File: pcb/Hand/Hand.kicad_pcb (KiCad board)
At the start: 4 copper layers, 76.2 x 50.8 mm, 43 parts, among them J0 Conn_01x12_Ribbon_Top, J1 Conn_01x12_Ribbon_Bottom, J2 Conn_01x02_Feedback_Power, U1 CD74HC4067M96, U2 4754, U3 TCA9548A

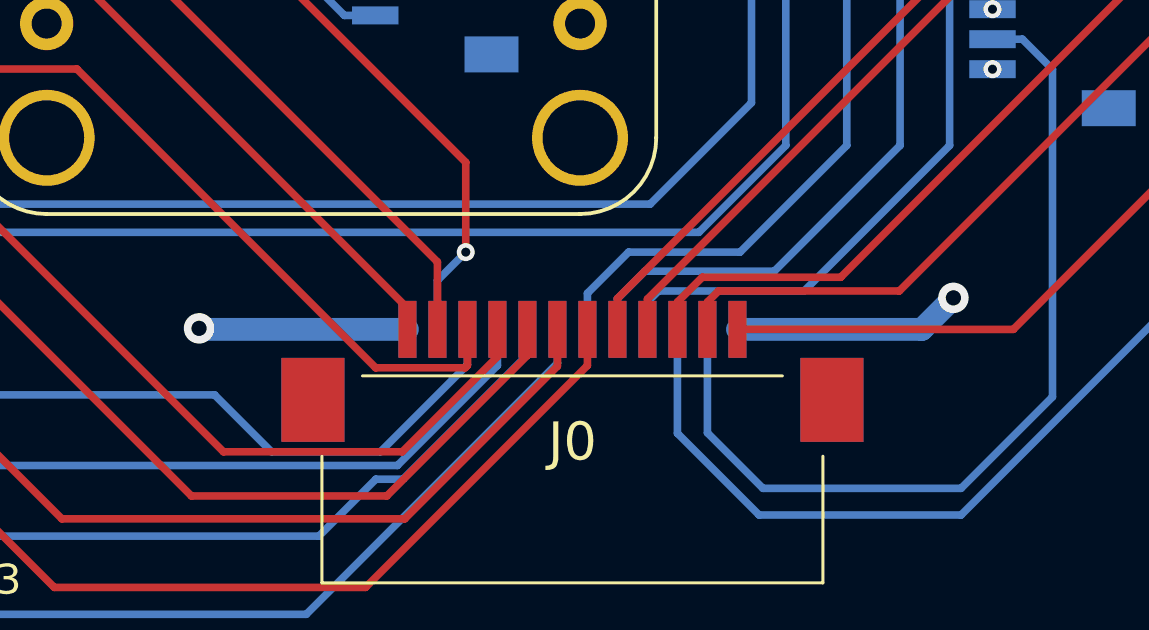
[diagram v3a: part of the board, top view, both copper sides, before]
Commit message: revised pcbs in preparation for pcb review; added pull-ups etc to forearm
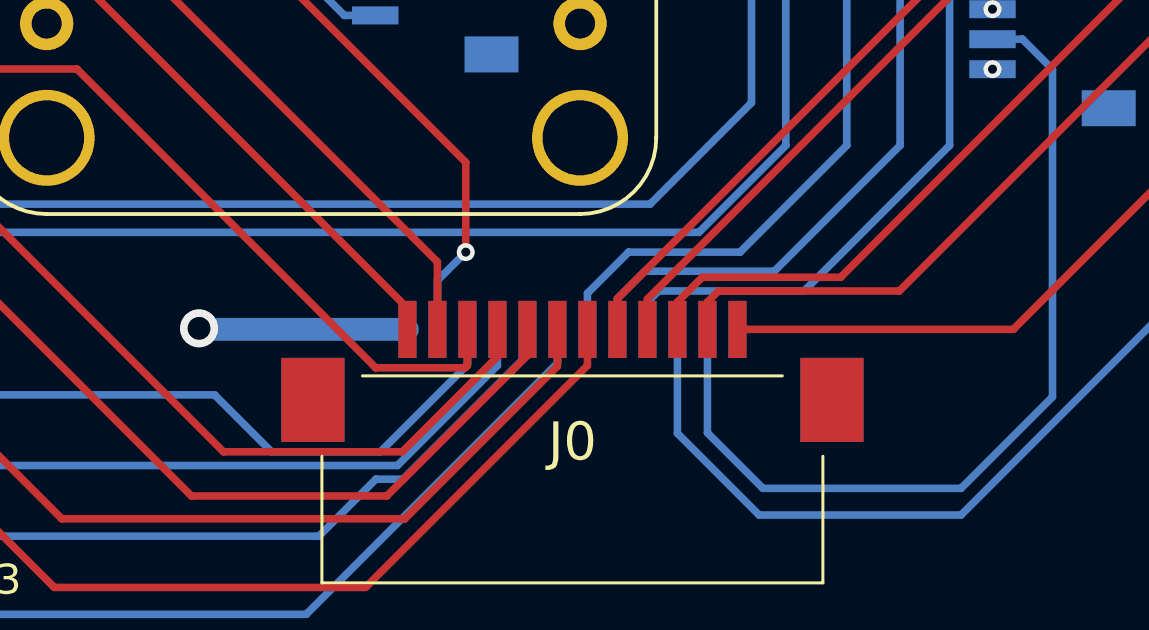
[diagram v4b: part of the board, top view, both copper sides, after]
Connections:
- FB0 pad 2: 6V0_GND -> GND
- FB1 pad 2: 6V0_GND -> GND
- FB2 pad 2: 6V0_GND -> GND
- FB3 pad 2: 6V0_GND -> GND
- FB4 pad 2: 6V0_GND -> GND
- J1 pad 1: GND -> FREE
- J2 pad 1: 6V0_GND -> GND
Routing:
- net GND: track 14.0 -> 6.37 mm, vias 29 -> 33
- net 6V0_GND: vias 5 -> 0
- removed copper zone on In2.Cu, net 6V0_GND
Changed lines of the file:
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@@
 	(net 50 "HALL_S1")
 	(net 51 "HALL_S3")
-	(net 52 "6V0_GND")
-	(net 53 "Net-(U1-~{E})")
-	(net 54 "unconnected-(U2-BT-PadJP2_1)")
-	(net 55 "unconnected-(U2-~{INT}-PadJP1_6)")
-	(net 56 "unconnected-(U2-~{RST}-PadJP2_4)")
-	(net 57 "unconnected-(U2-CS-PadJP2_6)")
-	(net 58 "unconnected-(U2-3VO-PadJP1_2)")
+	(net 52 "Net-(U1-~{E})")
+	(net 53 "unconnected-(U2-BT-PadJP2_1)")
+	(net 54 "unconnected-(U2-~{INT}-PadJP1_6)")
+	(net 55 "unconnected-(U2-~{RST}-PadJP2_4)")
+	(net 56 "unconnected-(U2-CS-PadJP2_6)")
+	(net 57 "unconnected-(U2-3VO-PadJP1_2)")
+	(net 58 "FREE")
 	(footprint "MountingHole:MountingHole_2.2mm_M2"
 		(layer "F.Cu")
@@
 			(size 0.6 1.55)
 			(layers "F.Cu" "F.Paste" "F.Mask")
-			(net 52 "6V0_GND")
+			(net 1 "GND")
 			(pinfunction "Pin_2")
 			(pintype "passive")
@@
 			(size 0.6 1.55)
 			(layers "F.Cu" "F.Paste" "F.Mask")
-			(net 52 "6V0_GND")
+			(net 1 "GND")
 			(pinfunction "Pin_2")
 			(pintype "passive")
@@
 			(layers "*.Cu" "*.Mask")
 			(remove_unused_layers no)
-			(net 52 "6V0_GND")
+			(net 1 "GND")
 			(pinfunction "Pin_1")
 			(pintype "passive")
@@
 			(size 0.6 1.55)
 			(layers "F.Cu" "F.Paste" "F.Mask")
-			(net 52 "6V0_GND")
+			(net 1 "GND")
 			(pinfunction "Pin_2")
 			(pintype "passive")
@@
 			(size 0.6 1.55)
 			(layers "F.Cu" "F.Paste" "F.Mask")
-			(net 52 "6V0_GND")
+			(net 1 "GND")
 			(pinfunction "Pin_2")
 			(pintype "passive")
@@
 			(size 0.6 1.55)
 			(layers "F.Cu" "F.Paste" "F.Mask")
-			(net 52 "6V0_GND")
+			(net 1 "GND")
 			(pinfunction "Pin_2")
 			(pintype "passive")
@@
 			(layers "*.Cu" "*.Mask")
 			(remove_unused_layers no)
-			(net 58 "unconnected-(U2-3VO-PadJP1_2)")
+			(net 57 "unconnected-(U2-3VO-PadJP1_2)")
 			(pinfunction "3VO")
 			(pintype "output")
@@
 			(layers "*.Cu" "*.Mask")
 			(remove_unused_layers no)
-			(net 55 "unconnected-(U2-~{INT}-PadJP1_6)")
+			(net 54 "unconnected-(U2-~{INT}-PadJP1_6)")
 			(pinfunction "~{INT}")
 			(pintype "output")
@@
 			(layers "*.Cu" "*.Mask")
 			(remove_unused_layers no)
-			(net 54 "unconnected-(U2-BT-PadJP2_1)")
+			(net 53 "unconnected-(U2-BT-PadJP2_1)")
 			(pinfunction "BT")
 			(pintype "input")
@@
 			(layers "*.Cu" "*.Mask")
 			(remove_unused_layers no)
-			(net 56 "unconnected-(U2-~{RST}-PadJP2_4)")
+			(net 55 "unconnected-(U2-~{RST}-PadJP2_4)")
 			(pinfunction "~{RST}")
 			(pintype "input")
@@
 			(layers "*.Cu" "*.Mask")
 			(remove_unused_layers no)
-			(net 57 "unconnected-(U2-CS-PadJP2_6)")
+			(net 56 "unconnected-(U2-CS-PadJP2_6)")
 			(pinfunction "CS")
 			(pintype "input")
@@
 			(layers "B.Cu" "B.Paste" "B.Mask")
 			(roundrect_rratio 0.125)
-			(net 53 "Net-(U1-~{E})")
+			(net 52 "Net-(U1-~{E})")
 			(pinfunction "~{E}")
 			(pintype "input")
@@
 			(size 0.6 1.9)
 			(layers "B.Cu" "B.Paste" "B.Mask")
-			(net 1 "GND")
+			(net 58 "FREE")
 			(pinfunction "Pin_1")
 			(pintype "passive")
@@
 			(layers "B.Cu" "B.Paste" "B.Mask")
 			(roundrect_rratio 0.25)
-			(net 53 "Net-(U1-~{E})")
+			(net 52 "Net-(U1-~{E})")
 			(pintype "passive")
 		)
@@
 	)
 	(via
+		(at 82.896 40.386)
+		(size 0.6)
+		(drill 0.3)
+		(layers "F.Cu" "B.Cu")
+		(net 1)
+	)
+	(via
 		(at 73.184 30.464)
 		(size 0.6)
@@
 	)
 	(via
+		(at 82.836 46.736)
+		(size 0.6)
+		(drill 0.3)
+		(layers "F.Cu" "B.Cu")
+		(net 1)
+	)
+	(via
 		(at 38.1508 28.702)
 		(size 0.6)
@@
 	)
 	(via
+		(at 82.896 34.036)
+		(size 0.6)
+		(drill 0.3)
+		(layers "F.Cu" "B.Cu")
+		(net 1)
+	)
+	(via
+		(at 82.836 21.336)
+		(size 0.6)
+		(drill 0.3)
+		(layers "F.Cu" "B.Cu")
+		(free yes)
+		(net 1)
+	)
+	(via
 		(at 45.75 17.591)
 		(size 0.6)
@@
 	)
 	(via
-		(at 71.882 51.816)
-		(size 1.016)
-		(drill 0.508)
+		(at 82.836 27.686)
+		(size 0.6)
+		(drill 0.3)
 		(layers "F.Cu" "B.Cu")
-		(free yes)
 		(net 1)
 	)
@@
 	)
 	(segment
-		(start 64.682 52.867)
-		(end 70.831 52.867)
-		(width 0.762)
-		(layer "B.Cu")
-		(net 1)
-	)
-	(segment
 		(start 18.163 26.289)
 		(end 17.1942 26.289)
@@
 	)
 	(segment
-		(start 70.831 52.867)
-		(end 71.882 51.816)
-		(width 0.762)
-		(layer "B.Cu")
-		(net 1)
-	)
-	(segment
 		(start 16.4208 28.6164)
 		(end 16.497 28.6926)
@@
 	(via
 		(at 46.736 52.832)
-		(size 1.016)
-		(drill 0.508)
+		(size 1.27)
+		(drill 0.762)
 		(layers "F.Cu" "B.Cu")
 		(free yes)
@@
 	)
 	(segment
-		(start 46.771 52.867)
-		(end 46.736 52.832)
-		(width 0.254)
+		(start 53.682 52.867)
+		(end 46.771 52.867)
+		(width 0.762)
 		(layer "B.Cu")
 		(net 2)
 	)
 	(segment
-		(start 53.682 52.867)
-		(end 46.771 52.867)
+		(start 46.771 52.867)
+		(end 46.736 52.832)
 		(width 0.762)
 		(layer "B.Cu")
@@
 		(net 51)
 	)
-	(via
-		(at 82.896 40.386)
-		(size 0.6)
-		(drill 0.3)
-		(layers "F.Cu" "B.Cu")
-		(net 52)
-	)
-	(via
-		(at 82.836 46.736)
-		(size 0.6)
-		(drill 0.3)
-		(layers "F.Cu" "B.Cu")
-		(net 52)
-	)
-	(via
-		(at 82.896 34.036)
-		(size 0.6)
-		(drill 0.3)
-		(layers "F.Cu" "B.Cu")
-		(net 52)
-	)
-	(via
-		(at 82.836 21.336)
-		(size 0.6)
-		(drill 0.3)
-		(layers "F.Cu" "B.Cu")
-		(net 52)
-	)
-	(via
-		(at 82.836 27.686)
-		(size 0.6)
-		(drill 0.3)
-		(layers "F.Cu" "B.Cu")
-		(net 52)
-	)
 	(segment
 		(start 24.3332 22.150699)
@@
 		(width 0.254)
 		(layer "B.Cu")
-		(net 53)
+		(net 52)
 	)
 	(segment
@@
 		(width 0.254)
 		(layer "B.Cu")
-		(net 53)
+		(net 52)
 	)
 	(segment
@@
 		(width 0.254)
 		(layer "B.Cu")
-		(net 53)
+		(net 52)
 	)
 	(zone
@@
 		(polygon
 			(pts
-				(xy 12.192 12.192) (xy 79.756 12.192) (xy 79.756 62.992) (xy 12.192 62.992)
-			)
-		)
-	)
-	(zone
-		(net 52)
-		(net_name "6V0_GND")
-		(layer "In2.Cu")
-		(hatch edge 0.5)
-		(priority 3)
-		(connect_pads
-			(clearance 0.5)
-		)
-		(min_thickness 0.25)
-		(filled_areas_thickness no)
-		(fill yes
-			(thermal_gap 0.5)
-			(thermal_bridge_width 0.5)
-		)
-		(polygon
-			(pts
-				(xy 80.264 12.192) (xy 80.264 62.992) (xy 88.392 62.992) (xy 88.392 12.192)
+				(xy 12.192 12.192) (xy 88.392 12.192) (xy 88.392 62.992) (xy 12.192 62.992)
 			)
 		)

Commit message: revised pcbs in prep for manufacture, rev2
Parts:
- removed J0: Conn_01x12_Ribbon_Top, 0522071233:0522071233
- removed J1: Conn_01x12_Ribbon_Bottom, 0522071233:0522071233
- added J3: Conn_01x16_Top, 522071633:CON_522071633_MOL, F.Cu at (61.2, 56.0)
- added J4: Conn_01x16_Bottom, 522071633:CON_522071633_MOL, B.Cu at (61.2, 56.0)
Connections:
- U2 pad JP1_6: unconnected-(U2-~{INT}-PadJP1_6) -> IMU_1_INT
- U2 pad JP2_4: unconnected-(U2-~{RST}-PadJP2_4) -> IMU_1_RST
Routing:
- net IMU_1_INT: track 0.00 -> 19.0 mm
- net IMU_1_RST: track 0.00 -> 16.4 mm
- net IMU_SCL: track 20.7 -> 35.1 mm
- net HAPTIC_S2: track 24.8 -> 35.2 mm
- net IMU_SDA: track 17.7 -> 27.9 mm
- net HAPTIC_S1: track 26.9 -> 34.6 mm
- net HAPTIC_S0: track 28.0 -> 34.7 mm
- net FEEDBACK_D4: track 21.1 -> 17.0 mm
- net HAPTIC_SDA: track 29.6 -> 33.5 mm, vias 0 -> 2
- net FEEDBACK_D3: track 25.3 -> 21.4 mm
- net FEEDBACK_D2: track 31.3 -> 27.4 mm
- net HAPTIC_SCL: track 27.8 -> 30.8 mm, vias 0 -> 2
- net FEEDBACK_D1: track 36.1 -> 34.4 mm
- net FEEDBACK_D0: track 42.2 -> 40.5 mm
- net unconnected-(J3-Pin_1-Pad1): track 0.00 -> 0.71 mm

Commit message: hand boatd final?
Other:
- board text added: "Dexterity Hand JLL"

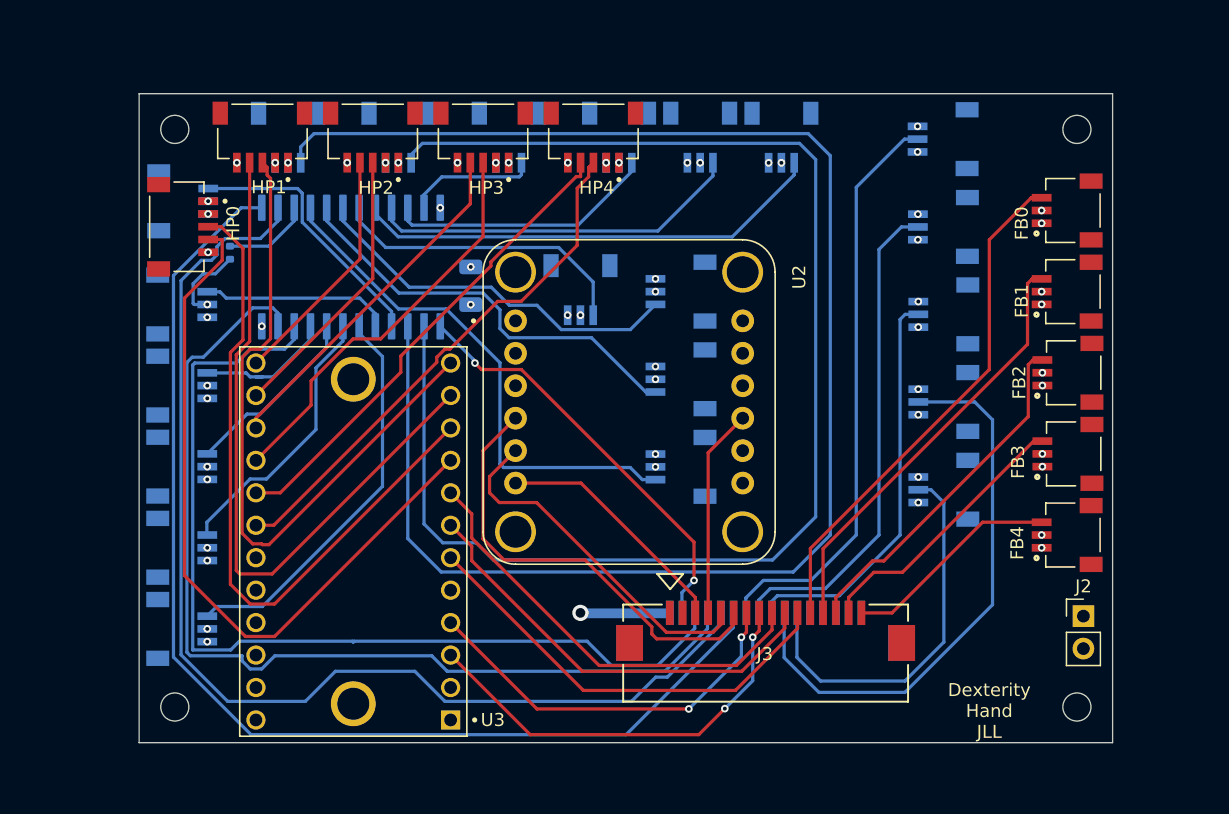
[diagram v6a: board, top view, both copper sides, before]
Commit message: added ground pours and generated gerbers for pcbs
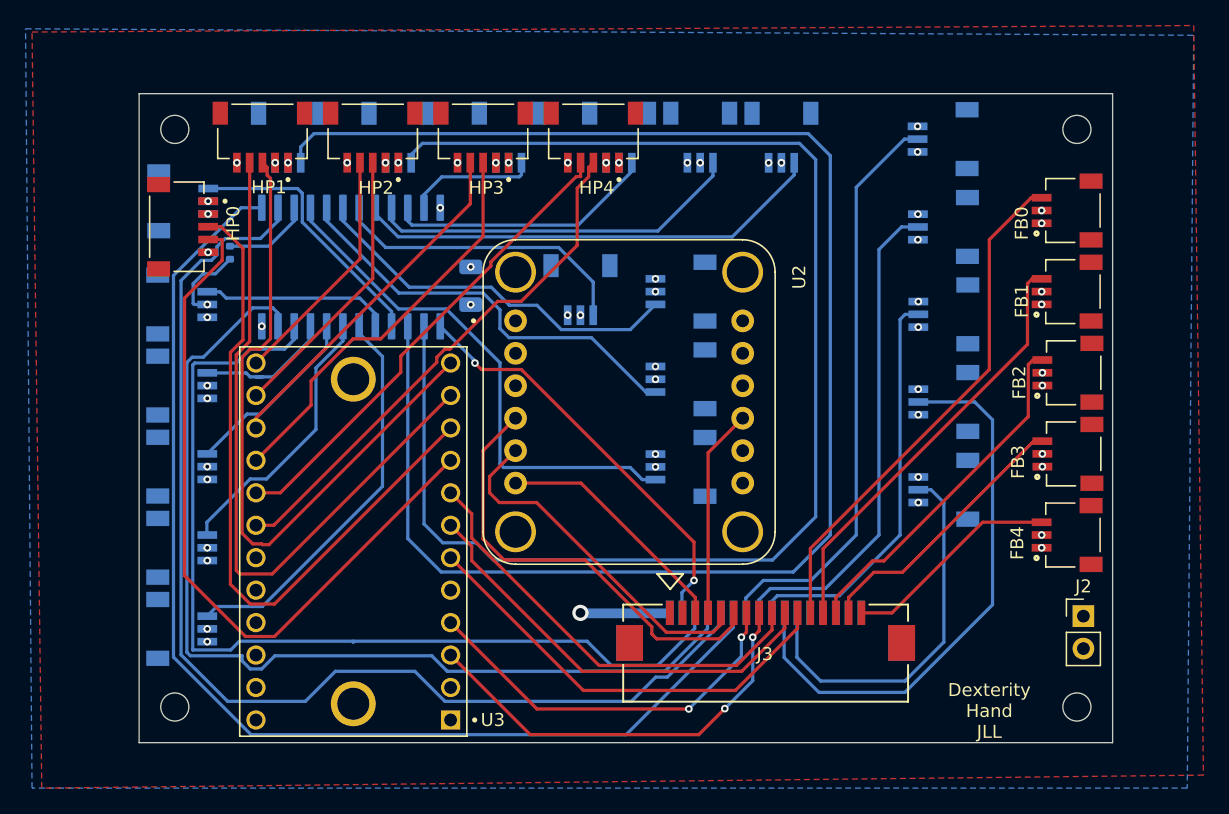
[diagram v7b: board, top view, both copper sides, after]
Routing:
- added copper zone on B.Cu, net GND
- added copper zone on F.Cu, net GND
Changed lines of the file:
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@@
 		(grid_origin 12.192 62.992)
 		(pcbplotparams
-			(layerselection 0x00000f0_ffffffff)
+			(layerselection 0x00010fc_ffffffff)
 			(plot_on_all_layers_selection 0x0000000_00000000)
 			(disableapertmacros no)
-			(usegerberextensions no)
-			(usegerberattributes yes)
-			(usegerberadvancedattributes yes)
-			(creategerberjobfile yes)
+			(usegerberextensions yes)
+			(usegerberattributes no)
+			(usegerberadvancedattributes no)
+			(creategerberjobfile no)
 			(dashed_line_dash_ratio 12.000000)
 			(dashed_line_gap_ratio 3.000000)
@@
 			(plotinvisibletext no)
 			(sketchpadsonfab no)
-			(subtractmaskfromsilk no)
+			(subtractmaskfromsilk yes)
 			(outputformat 1)
 			(mirror no)
 			(drillshape 0)
 			(scaleselection 1)
-			(outputdirectory "/Users/jacksonlamb/Desktop/suck my cock/")
+			(outputdirectory "/Users/jacksonlamb/Desktop/hand")
 		)
 	)
@@
 	)
 	(zone
+		(net 1)
+		(net_name "GND")
+		(layer "F.Cu")
+		(hatch edge 0.5)
+		(priority 3)
+		(connect_pads
+			(clearance 0.5)
+		)
+		(min_thickness 0.25)
+		(filled_areas_thickness no)
+		(fill yes
+			(thermal_gap 0.5)
+			(thermal_bridge_width 0.5)
+		)
+		(polygon
+			(pts
+				(xy 3.81 7.366) (xy 94.742 6.858) (xy 95.504 65.532) (xy 4.572 66.548)
+			)
+		)
+	)
+	(zone
 		(net 2)
 		(net_name "3V3")
@@
 			)
 		)
+	)
+	(zone
+		(net 1)
+		(net_name "GND")
+		(layer "B.Cu")
+		(hatch edge 0.5)
+		(priority 4)
+		(connect_pads
+			(clearance 0.5)
+		)
+		(min_thickness 0.25)
+		(filled_areas_thickness no)
+		(fill yes
+			(thermal_gap 0.5)
+			(thermal_bridge_width 0.5)
+		)
+		(polygon
+			(pts
+				(xy 3.302 7.112) (xy 94.742 7.62) (xy 94.234 66.548) (xy 3.81 66.548)
+			)
+		)
